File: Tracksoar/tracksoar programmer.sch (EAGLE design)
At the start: 12 parts, among them U1 FT232RL-BASICSSOP

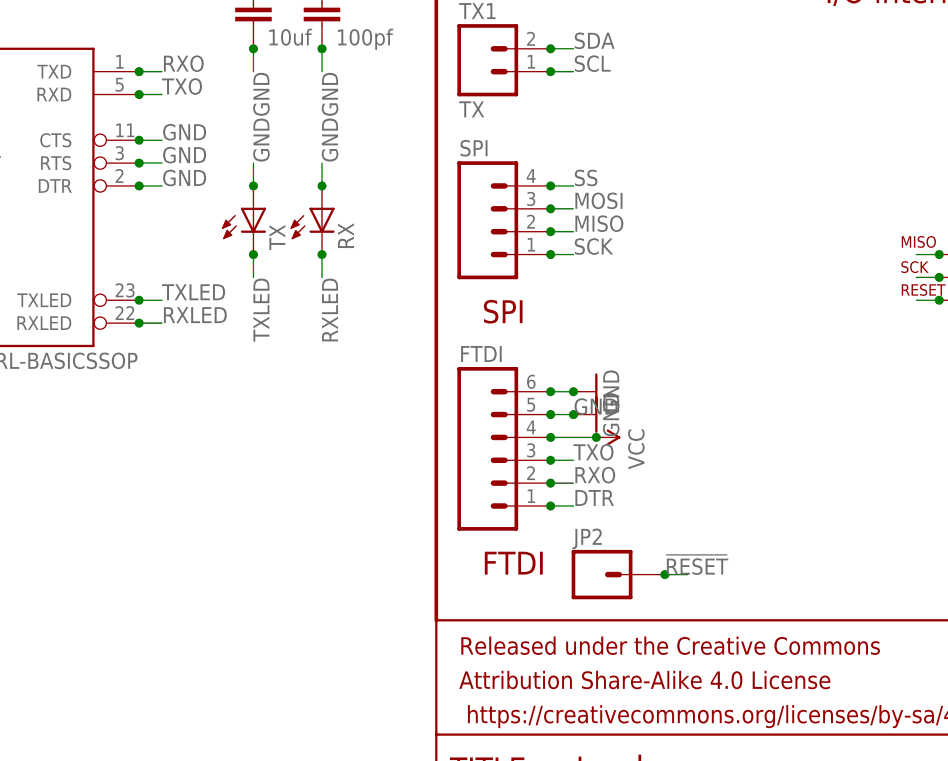
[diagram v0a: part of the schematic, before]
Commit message: replace headers
replaced 2.54mm headers on all production boards with 2mm headers to
resolve daughter board issues.
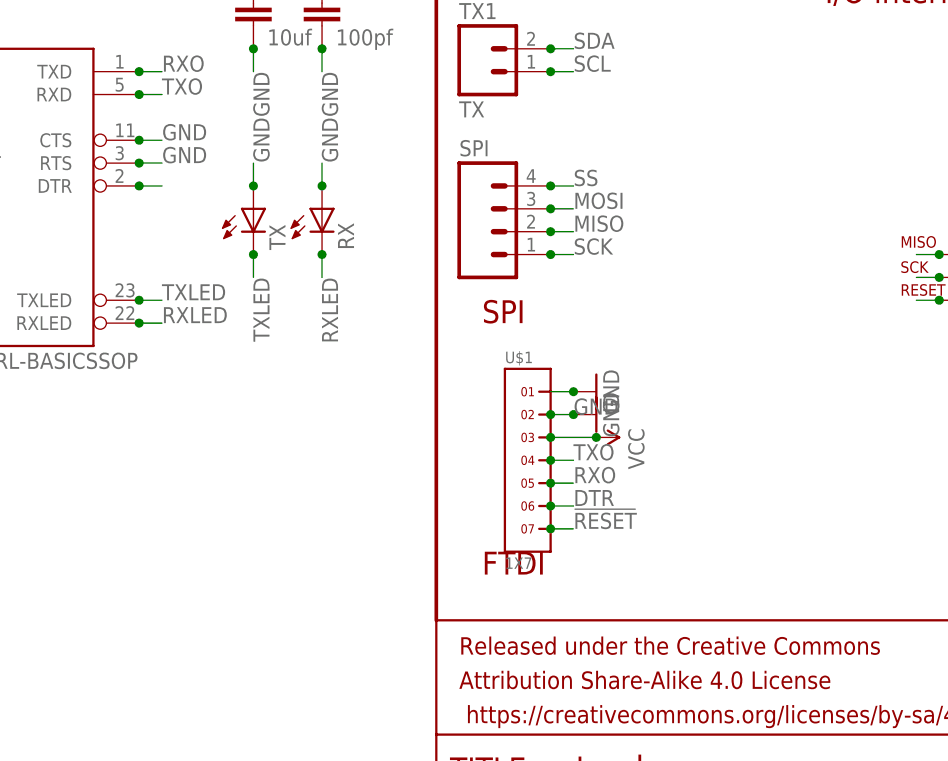
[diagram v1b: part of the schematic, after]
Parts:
- removed FTDI: (no value), SparkFun-Connectors:M06NO_SILK_FEMALE_PTH
- removed JP2: (no value), SparkFun-Connectors:M01PTH
- added U$1: 1X7, headers(2mm):1X7
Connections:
- net !RESET: now also U$1.7; no longer JP2.1
- net DTR: now also U$1.6, U1.DTR; no longer FTDI.1
- net GND: now also U$1.1, U$1.2; no longer FTDI.5, FTDI.6, U1.DTR
- net RXO: now also U$1.5; no longer FTDI.2
- net TXO: now also U$1.4; no longer FTDI.3
- net VCC: now also U$1.3; no longer FTDI.4
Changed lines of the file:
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@@
 </classes>
 <parts>
-<part name="FTDI" library="SparkFun-Connectors" deviceset="M06" device="NO_SILK_FEMALE_PTH"/>
 <part name="GND22" library="SparkFun-Aesthetics" deviceset="GND" device=""/>
 <part name="SUPPLY9" library="SparkFun-Aesthetics" deviceset="VCC" device=""/>
@@
 <part name="GND10" library="SparkFun-Aesthetics" deviceset="GND" device=""/>
 <part name="TX1" library="SparkFun-Connectors" deviceset="M02" device="JST-PTH-VERT" value="TX"/>
-<part name="JP2" library="SparkFun-Connectors" deviceset="M01" device="PTH"/>
 <part name="ICSP" library="SparkFun-Connectors" deviceset="AVR_SPI_PRG_6" device="PTH"/>
 <part name="SUPPLY1" library="SparkFun-Aesthetics" deviceset="VCC" device=""/>
@@
 <part name="TX" library="adafruit" deviceset="LED" device="CHIP-LED0805"/>
 <part name="RX" library="adafruit" deviceset="LED" device="CHIP-LED0805"/>
+<part name="U$1" library="headers(2mm)" deviceset="1X7" device=""/>
 </parts>
 <sheets>
@@
 </plain>
 <instances>
-<instance part="FTDI" gate="G$1" x="154.94" y="53.34"/>
 <instance part="GND22" gate="1" x="165.1" y="60.96" rot="R90"/>
 <instance part="SUPPLY9" gate="G$1" x="165.1" y="55.88" rot="R270"/>
@@
 <instance part="GND10" gate="1" x="165.1" y="58.42" rot="R90"/>
 <instance part="TX1" gate="G$1" x="152.4" y="96.52"/>
-<instance part="JP2" gate="G$1" x="165.1" y="40.64"/>
 <instance part="ICSP" gate="G$1" x="210.82" y="73.66"/>
 <instance part="SUPPLY1" gate="G$1" x="220.98" y="76.2" rot="R270"/>
@@
 <instance part="TX" gate="G$1" x="127" y="81.28"/>
 <instance part="RX" gate="G$1" x="134.62" y="81.28"/>
+<instance part="U$1" gate="G$1" x="157.48" y="53.34"/>
 </instances>
 <busses>
@@
 <net name="GND" class="0">
 <segment>
-<pinref part="FTDI" gate="G$1" pin="6"/>
 <wire x1="160.02" y1="60.96" x2="162.56" y2="60.96" width="0.1524" layer="91"/>
 <pinref part="GND22" gate="1" pin="GND"/>
-<junction x="160.02" y="60.96"/>
 <junction x="162.56" y="60.96"/>
-</segment>
-<segment>
-<pinref part="FTDI" gate="G$1" pin="5"/>
+<pinref part="U$1" gate="G$1" pin="1"/>
+</segment>
+<segment>
 <wire x1="160.02" y1="58.42" x2="162.56" y2="58.42" width="0.1524" layer="91"/>
 <label x="162.56" y="58.42" size="1.778" layer="95"/>
-<junction x="160.02" y="58.42"/>
 <pinref part="GND10" gate="1" pin="GND"/>
 <junction x="162.56" y="58.42"/>
+<pinref part="U$1" gate="G$1" pin="2"/>
+<junction x="160.02" y="58.42"/>
 </segment>
 <segment>
@@
 <junction x="114.3" y="86.36"/>
 <label x="116.84" y="86.36" size="1.778" layer="95"/>
-</segment>
-<segment>
-<pinref part="U1" gate="G$1" pin="DTR"/>
-<wire x1="114.3" y1="83.82" x2="116.84" y2="83.82" width="0.1524" layer="91"/>
-<junction x="114.3" y="83.82"/>
-<label x="116.84" y="83.82" size="1.778" layer="95"/>
 </segment>
 <segment>
@@
 <net name="VCC" class="0">
 <segment>
-<pinref part="FTDI" gate="G$1" pin="4"/>
 <wire x1="160.02" y1="55.88" x2="165.1" y2="55.88" width="0.1524" layer="91"/>
 <pinref part="SUPPLY9" gate="G$1" pin="VCC"/>
+<junction x="165.1" y="55.88"/>
+<pinref part="U$1" gate="G$1" pin="3"/>
 <junction x="160.02" y="55.88"/>
-<junction x="165.1" y="55.88"/>
 </segment>
 <segment>
@@
 <net name="DTR" class="0">
 <segment>
-<pinref part="FTDI" gate="G$1" pin="1"/>
 <wire x1="160.02" y1="48.26" x2="162.56" y2="48.26" width="0.1524" layer="91"/>
 <label x="162.56" y="48.26" size="1.778" layer="95"/>
+<pinref part="U$1" gate="G$1" pin="6"/>
 <junction x="160.02" y="48.26"/>
 </segment>
+<segment>
+<pinref part="U1" gate="G$1" pin="DTR"/>
+<wire x1="114.3" y1="83.82" x2="116.84" y2="83.82" width="0.1524" layer="91"/>
+<junction x="114.3" y="83.82"/>
+</segment>
 </net>
 <net name="RXO" class="0">
 <segment>
-<pinref part="FTDI" gate="G$1" pin="2"/>
 <wire x1="160.02" y1="50.8" x2="162.56" y2="50.8" width="0.1524" layer="91"/>
 <label x="162.56" y="50.8" size="1.778" layer="95"/>
+<pinref part="U$1" gate="G$1" pin="5"/>
 <junction x="160.02" y="50.8"/>
 </segment>
@@
 <net name="TXO" class="0">
 <segment>
-<pinref part="FTDI" gate="G$1" pin="3"/>
 <wire x1="160.02" y1="53.34" x2="162.56" y2="53.34" width="0.1524" layer="91"/>
 <label x="162.56" y="53.34" size="1.778" layer="95"/>
+<pinref part="U$1" gate="G$1" pin="4"/>
 <junction x="160.02" y="53.34"/>
 </segment>
@@
 <net name="!RESET" class="0">
 <segment>
-<pinref part="JP2" gate="G$1" pin="1"/>
-<wire x1="172.72" y1="40.64" x2="175.26" y2="40.64" width="0.1524" layer="91"/>
-<label x="172.72" y="40.64" size="1.778" layer="95"/>
-<junction x="172.72" y="40.64"/>
-</segment>
-<segment>
+<wire x1="160.02" y1="45.72" x2="162.56" y2="45.72" width="0.1524" layer="91"/>
+<label x="162.56" y="45.72" size="1.778" layer="95"/>
+<pinref part="U$1" gate="G$1" pin="7"/>
+<junction x="160.02" y="45.72"/>
+</segment>
+<segment>
